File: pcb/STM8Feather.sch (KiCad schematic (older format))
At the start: 29 parts, among them J1 feather long, J2 feather short, J3 USB_B_Micro, J4 Conn_01x02, J5 Conn_01x04, U1 STM8S003K3T, U2 MCP73831-2-OT, U3 MIC5504-3.3YM5, U4 CH330N, Y1 Crystal

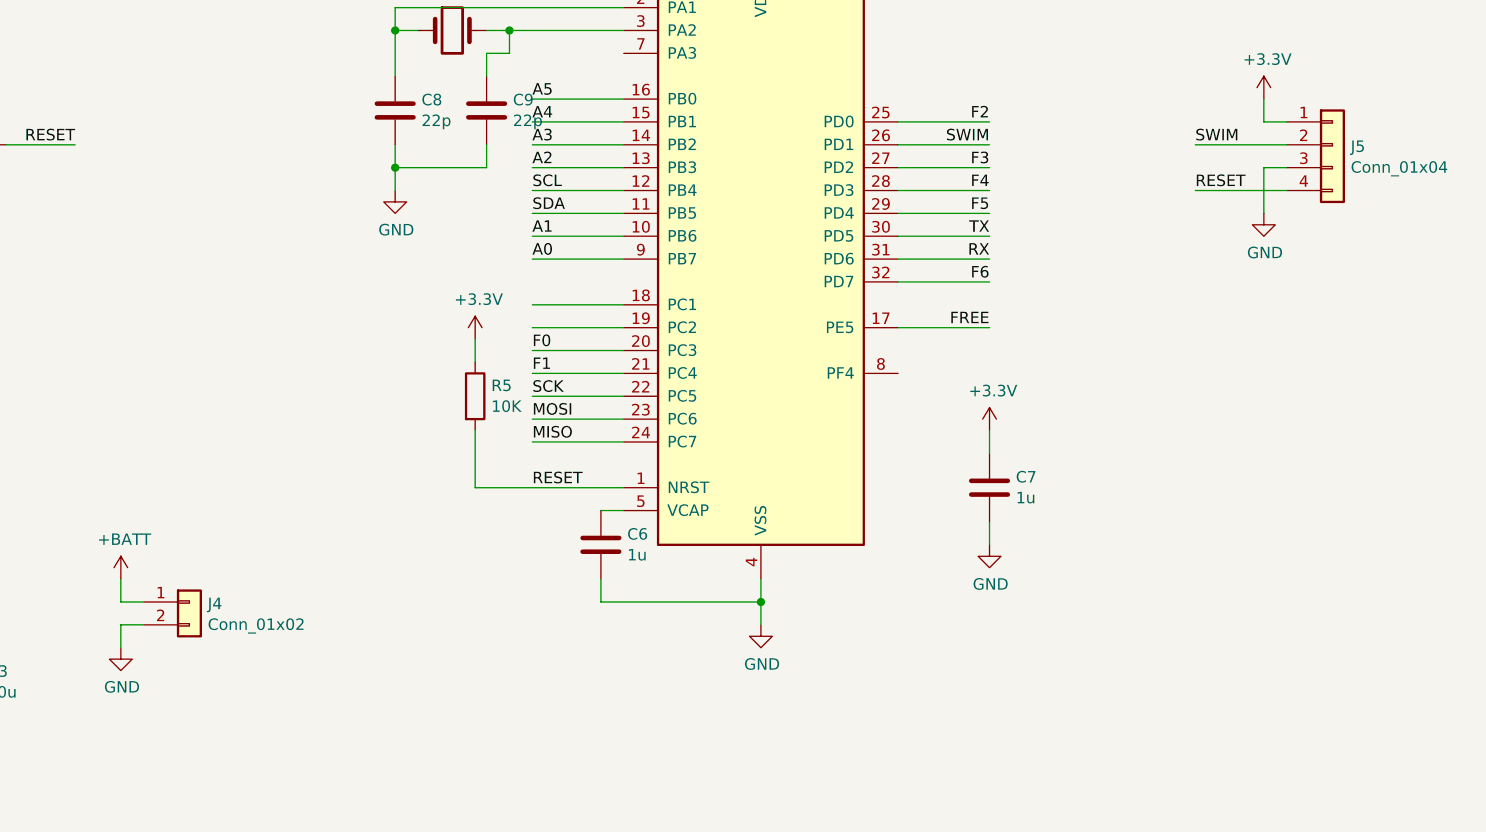
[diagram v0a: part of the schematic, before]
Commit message: Adding status LED, reset button, boot button, and power LED
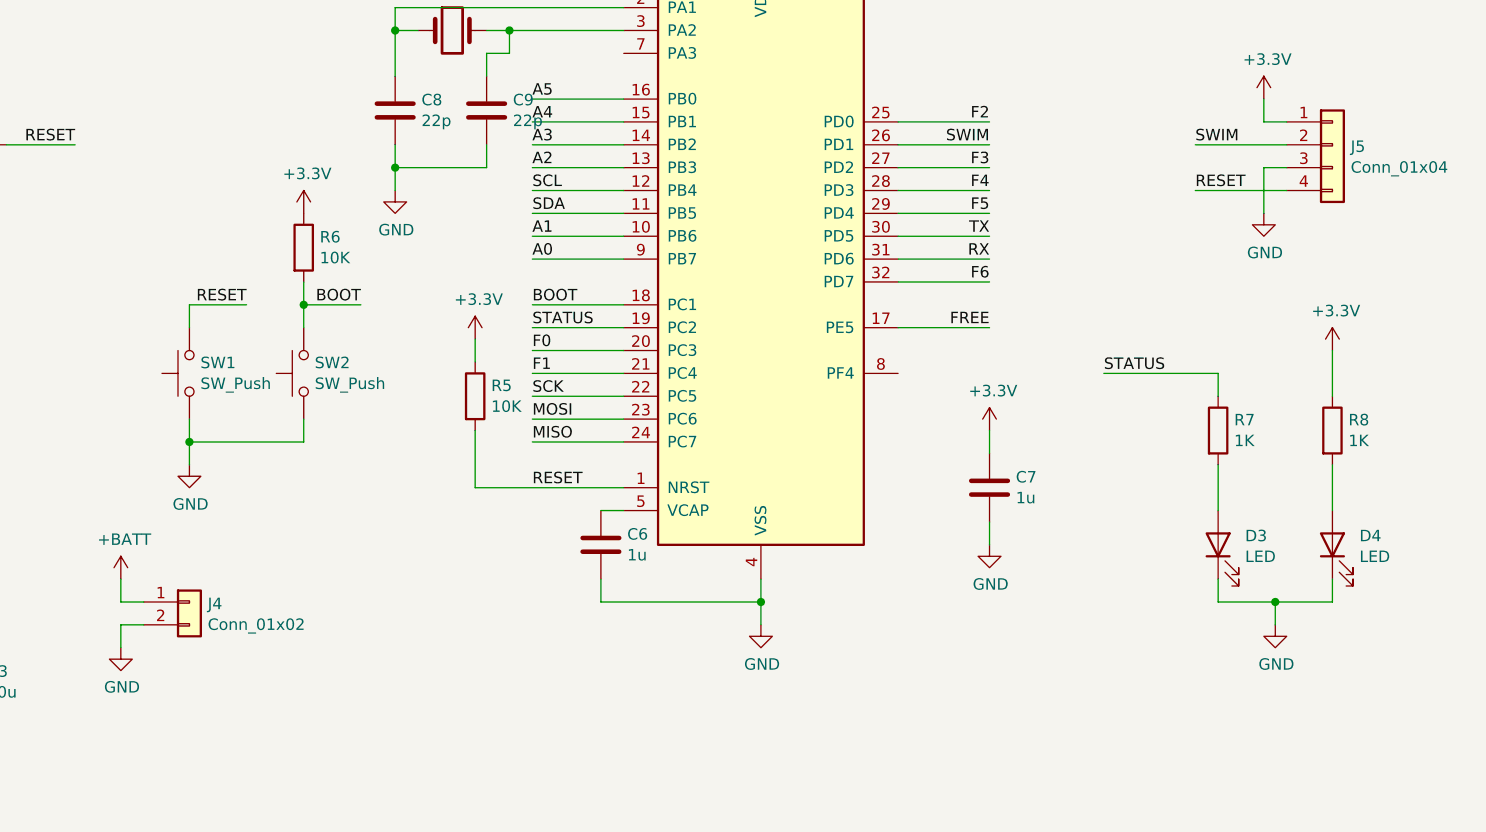
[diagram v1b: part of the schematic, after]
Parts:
- added D3, D4: LED, LED_SMD:LED_0603_1608Metric, symbol Device:LED
- added R6: 10K, Resistor_SMD:R_0603_1608Metric, symbol Device:R
- added R7, R8: 1K, Resistor_SMD:R_0603_1608Metric, symbol Device:R
- added SW1, SW2: SW_Push, Button_Switch_SMD:SW_Push_SPST_NO_Alps_SKRK, symbol Switch:SW_Push
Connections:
- net +3V3: now also R6.1, R8.1
- net GND: now also D3.1 (K), D4.1 (K), SW1.1, SW2.1
- net RESET: now also SW1.2
- net BOOT: now reaches U1.18 (PC1)
- net BOOT: now also R6.2, SW2.2
- net STATUS: now reaches U1.19 (PC2)
- net STATUS: now also R7.1
- new net: D3.2 (A), R7.2
- new net: D4.2 (A), R8.2
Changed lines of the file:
@@
 	2700 5000 2900 5000
 Connection ~ 2900 5000
+Text Label 6500 5200 0    50   ~ 0
+BOOT
+Text Label 6500 5300 0    50   ~ 0
+STATUS
+$Comp
+L Switch:SW_Push SW1
+U 1 1 605DCCFA
+P 5000 5500
+F 0 "SW1" V 5046 5452 50  0000 R CNN
+F 1 "SW_Push" V 4955 5452 50  0000 R CNN
+F 2 "Button_Switch_SMD:SW_Push_SPST_NO_Alps_SKRK" H 5000 5700 50  0001 C CNN
+F 3 "~" H 5000 5700 50  0001 C CNN
+	1    5000 5500
+	0    -1   -1   0
+$EndComp
+$Comp
+L Switch:SW_Push SW2
+U 1 1 605DD194
+P 5500 5500
+F 0 "SW2" V 5546 5452 50  0000 R CNN
+F 1 "SW_Push" V 5455 5452 50  0000 R CNN
+F 2 "Button_Switch_SMD:SW_Push_SPST_NO_Alps_SKRK" H 5500 5700 50  0001 C CNN
+F 3 "~" H 5500 5700 50  0001 C CNN
+	1    5500 5500
+	0    -1   -1   0
+$EndComp
+Text Label 5250 5200 2    50   ~ 0
+RESET
+Text Label 5750 5200 2    50   ~ 0
+BOOT
+$Comp
+L Device:R R6
+U 1 1 605DD505
+P 5500 4950
+F 0 "R6" H 5570 4996 50  0000 L CNN
+F 1 "10K" H 5570 4905 50  0000 L CNN
+F 2 "Resistor_SMD:R_0603_1608Metric" V 5430 4950 50  0001 C CNN
+F 3 "~" H 5500 4950 50  0001 C CNN
+	1    5500 4950
+	1    0    0    -1
+$EndComp
+$Comp
+L power:+3.3V #PWR0124
+U 1 1 605DD79B
+P 5500 4800
+F 0 "#PWR0124" H 5500 4650 50  0001 C CNN
+F 1 "+3.3V" H 5515 4973 50  0000 C CNN
+F 2 "" H 5500 4800 50  0001 C CNN
+F 3 "" H 5500 4800 50  0001 C CNN
+	1    5500 4800
+	1    0    0    -1
+$EndComp
+Wire Wire Line
+	5250 5200 5000 5200
+Wire Wire Line
+	5000 5200 5000 5300
+Wire Wire Line
+	5750 5200 5500 5200
+Wire Wire Line
+	5500 5200 5500 5300
+Wire Wire Line
+	5500 5100 5500 5200
+Connection ~ 5500 5200
+$Comp
+L power:GND #PWR0125
+U 1 1 60600936
+P 5000 5900
+F 0 "#PWR0125" H 5000 5650 50  0001 C CNN
+F 1 "GND" H 5005 5727 50  0000 C CNN
+F 2 "" H 5000 5900 50  0001 C CNN
+F 3 "" H 5000 5900 50  0001 C CNN
+	1    5000 5900
+	1    0    0    -1
+$EndComp
+Wire Wire Line
+	5000 5700 5000 5800
+Wire Wire Line
+	5000 5800 5500 5800
+Wire Wire Line
+	5500 5800 5500 5700
+Connection ~ 5000 5800
+Wire Wire Line
+	5000 5800 5000 5900
+Text Label 9000 5500 0    50   ~ 0
+STATUS
+$Comp
+L Device:LED D3
+U 1 1 606136D0
+P 9500 6250
+F 0 "D3" V 9539 6132 50  0000 R CNN
+F 1 "LED" V 9448 6132 50  0000 R CNN
+F 2 "LED_SMD:LED_0603_1608Metric" H 9500 6250 50  0001 C CNN
+F 3 "~" H 9500 6250 50  0001 C CNN
+	1    9500 6250
+	0    -1   -1   0
+$EndComp
+$Comp
+L Device:R R7
+U 1 1 60613FE5
+P 9500 5750
+F 0 "R7" H 9570 5796 50  0000 L CNN
+F 1 "1K" H 9570 5705 50  0000 L CNN
+F 2 "Resistor_SMD:R_0603_1608Metric" V 9430 5750 50  0001 C CNN
+F 3 "~" H 9500 5750 50  0001 C CNN
+	1    9500 5750
+	1    0    0    -1
+$EndComp
+$Comp
+L Device:R R8
+U 1 1 60614898
+P 10000 5750
+F 0 "R8" H 10070 5796 50  0000 L CNN
+F 1 "1K" H 10070 5705 50  0000 L CNN
+F 2 "Resistor_SMD:R_0603_1608Metric" V 9930 5750 50  0001 C CNN
+F 3 "~" H 10000 5750 50  0001 C CNN
+	1    10000 5750
+	1    0    0    -1
+$EndComp
+$Comp
+L Device:LED D4
+U 1 1 60614AA1
+P 10000 6250
+F 0 "D4" V 10039 6132 50  0000 R CNN
+F 1 "LED" V 9948 6132 50  0000 R CNN
+F 2 "LED_SMD:LED_0603_1608Metric" H 10000 6250 50  0001 C CNN
+F 3 "~" H 10000 6250 50  0001 C CNN
+	1    10000 6250
+	0    -1   -1   0
+$EndComp
+$Comp
+L power:+3.3V #PWR0126
+U 1 1 60614D74
+P 10000 5400
+F 0 "#PWR0126" H 10000 5250 50  0001 C CNN
+F 1 "+3.3V" H 10015 5573 50  0000 C CNN
+F 2 "" H 10000 5400 50  0001 C CNN
+F 3 "" H 10000 5400 50  0001 C CNN
+	1    10000 5400
+	1    0    0    -1
+$EndComp
+Wire Wire Line
+	10000 5400 10000 5600
+Wire Wire Line
+	9000 5500 9500 5500
+Wire Wire Line
+	9500 5500 9500 5600
+Wire Wire Line
+	9500 5900 9500 6100
+Wire Wire Line
+	10000 6100 10000 5900
+$Comp
+L power:GND #PWR0127
+U 1 1 6063B36B
+P 9750 6600
+F 0 "#PWR0127" H 9750 6350 50  0001 C CNN
+F 1 "GND" H 9755 6427 50  0000 C CNN
+F 2 "" H 9750 6600 50  0001 C CNN
+F 3 "" H 9750 6600 50  0001 C CNN
+	1    9750 6600
+	1    0    0    -1
+$EndComp
+Wire Wire Line
+	9500 6400 9500 6500
+Wire Wire Line
+	9500 6500 9750 6500
+Wire Wire Line
+	9750 6500 9750 6600
+Wire Wire Line
+	9750 6500 10000 6500
+Wire Wire Line
+	10000 6500 10000 6400
+Connection ~ 9750 6500
 $EndSCHEMATC
